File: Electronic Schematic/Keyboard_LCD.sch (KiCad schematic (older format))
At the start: 12 parts, among them J10 PIC Programming Setup, J11 Ext. PIC Programmer Conn., U2 4022, U6 NE555P, U7 PIC16F84A-XXP, Y2 8MHz

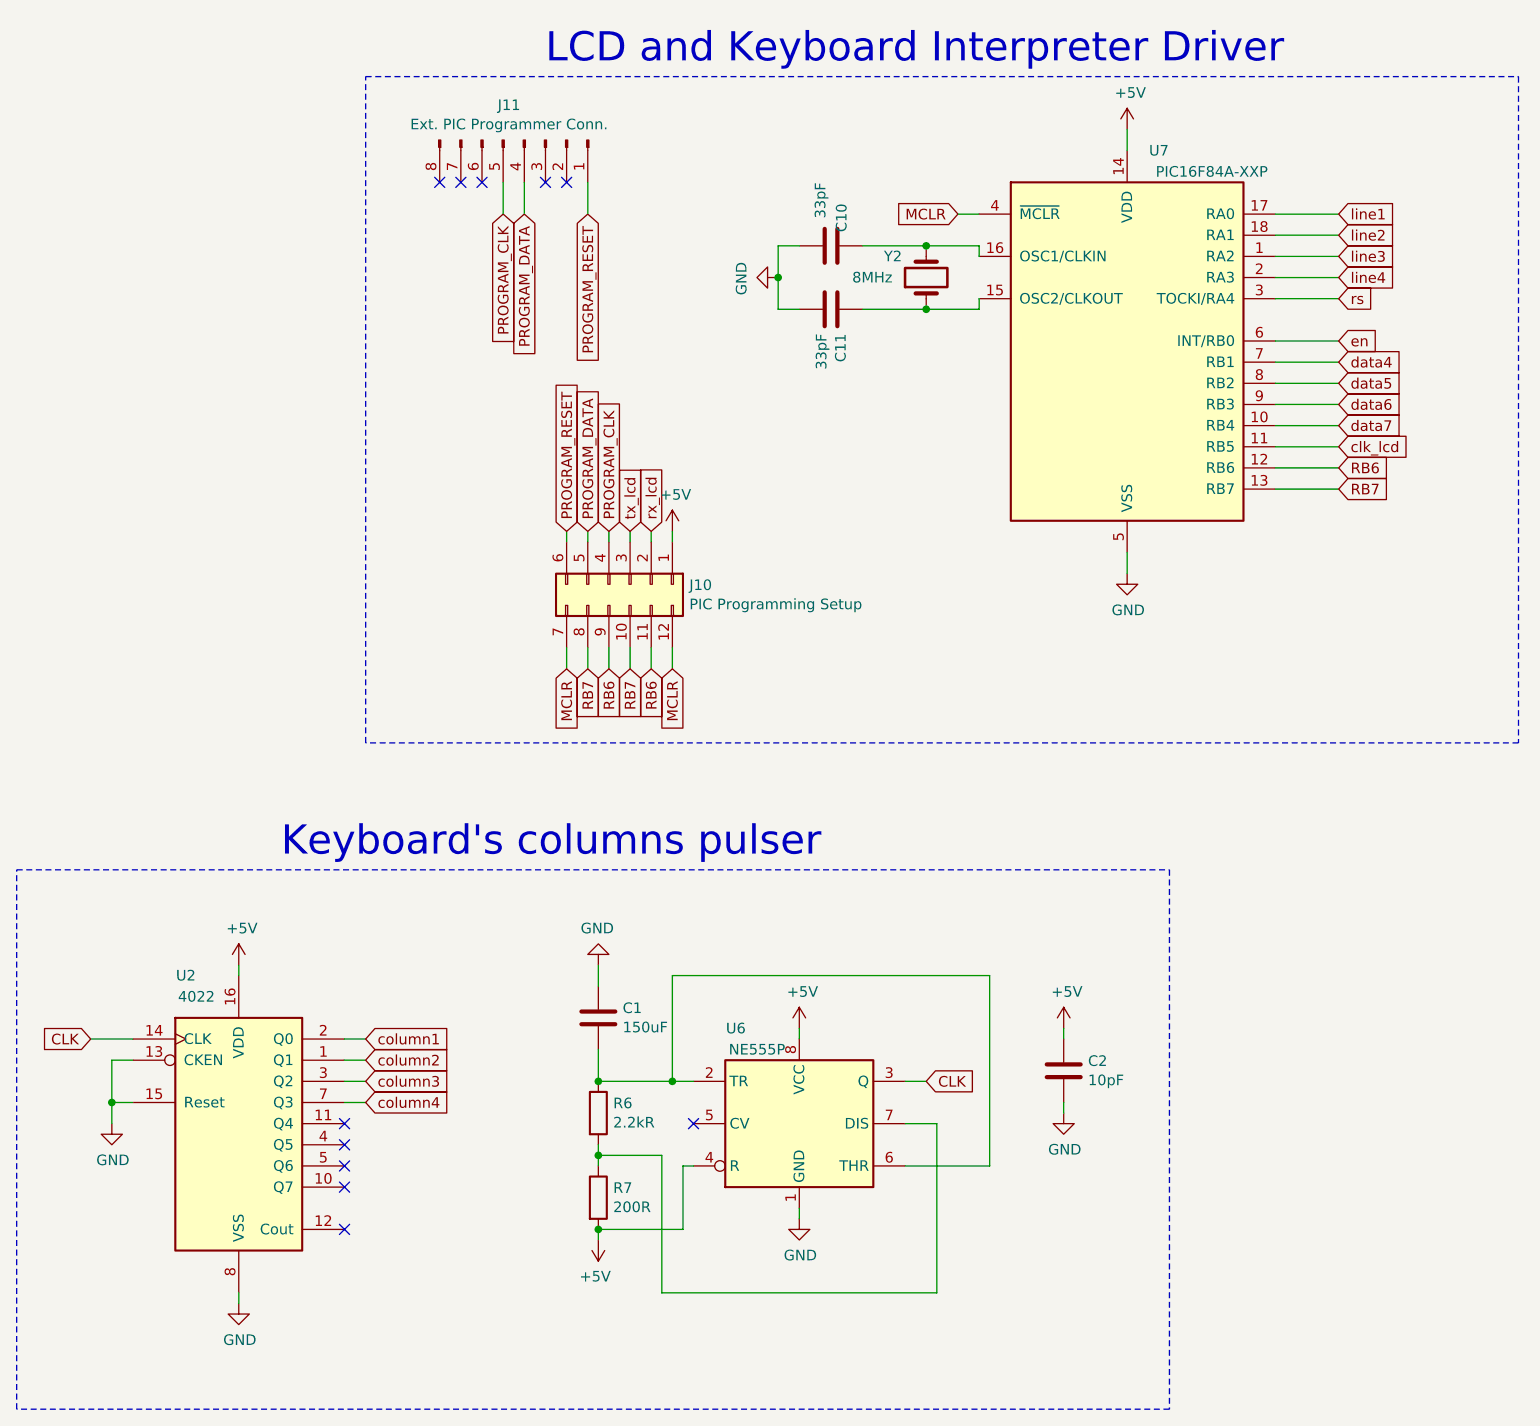
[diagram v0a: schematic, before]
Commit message: Correcoes Esquematico e Avanço codigo esp
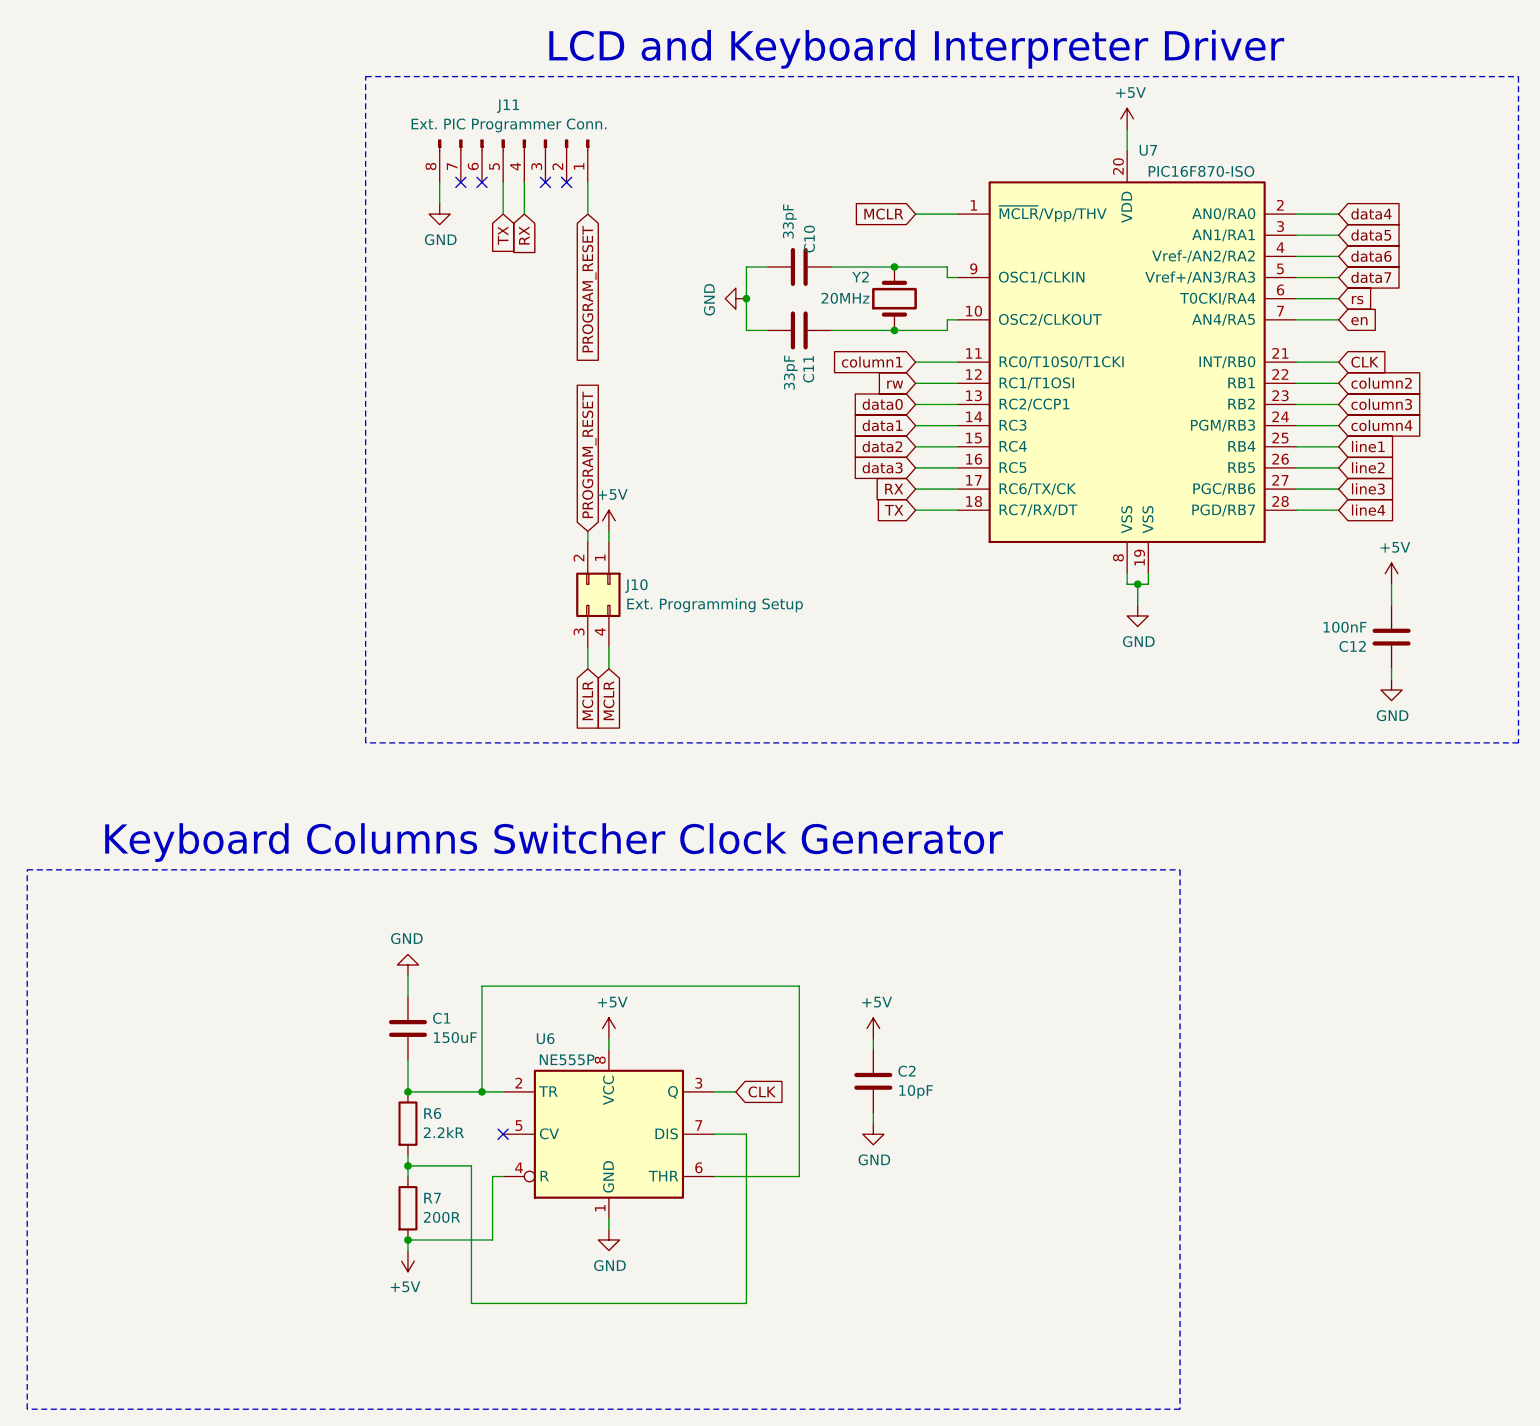
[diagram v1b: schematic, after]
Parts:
- removed J10: PIC Programming Setup, symbol Connector_Generic:Conn_02x06_Counter_Clockwise
- removed U2: 4022, symbol 4xxx:4022
- removed U7: PIC16F84A-XXP, symbol MCU_Microchip_PIC16:PIC16F84A-XXP
- added C12: 100nF, symbol Device:C
- added J10: Ext. Programming Setup, symbol Connector_Generic:Conn_02x02_Counter_Clockwise
- added U7: PIC16F870-ISO, symbol MCU_Microchip_PIC16:PIC16F870-ISO
- Y2: value 8MHz -> 20MHz
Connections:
- net +5V: now also C12.2, J10.1 (Pin_1), U7.20 (VDD)
- net CLK: now also U7.21 (INT/RB0)
- net GND: now also J11.8 (Pin_8), C12.1, U7.19 (VSS), U7.8 (VSS)
- net MCLR: now also J10.3 (Pin_3), J10.4 (Pin_4), U7.1 (~MCLR~/Vpp/THV)
- net PROGRAM_RESET: now also J10.2 (Pin_2)
- net column1: now also U7.11 (RC0/T10S0/T1CKI)
- net column2: now also U7.22 (RB1)
- net column3: now also U7.23 (RB2)
- net column4: now also U7.24 (PGM/RB3)
- net data4: now also U7.2 (AN0/RA0)
- net data5: now also U7.3 (AN1/RA1)
- net data6: now also U7.4 (Vref-/AN2/RA2)
- net data7: now also U7.5 (Vref+/AN3/RA3)
- net en: now also U7.7 (AN4/RA5)
- net line1: now also U7.25 (RB4)
- net line2: now also U7.26 (RB5)
- net line3: now also U7.27 (PGC/RB6)
- net line4: now also U7.28 (PGD/RB7)
- net rs: now also U7.6 (T0CKI/RA4)
- net at C11.1, Y2.1: now also U7.10 (OSC2/CLKOUT)
- net at C10.1, Y2.2: now also U7.9 (OSC1/CLKIN)
- net PROGRAM_CLK renamed TX
- net TX: now also U7.18 (RC7/RX/DT)
- net PROGRAM_DATA renamed RX
- net RX: now also U7.17 (RC6/TX/CK)
- new net data0: U7.13 (RC2/CCP1)
- new net data1: U7.14 (RC3)
- new net data2: U7.15 (RC4)
- new net data3: U7.16 (RC5)
- new net rw: U7.12 (RC1/T1OSI)
- no-connect marks 11 -> 5
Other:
- note added: "Keyboard Columns Switcher Clock Generator\n"
- note removed: "Keyboard's columns pulser\n"
- moved on the sheet: C1, C10, C11, C2, R6, R7, U6, Y2
